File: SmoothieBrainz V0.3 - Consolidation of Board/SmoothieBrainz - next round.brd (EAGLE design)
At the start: 101 x 101 mm, 219 parts, among them IC1 LPC1769, IC5 LD117ADT33TR, Q1 BSL207SP, Q2 12MHz, SW1 SW_TACT_4P_B, SW3 SW_TACT_4P_B, T1 BC817, U3 USD-SOCKETUSD, X1 MSTBA2, X14 USBPTH, X2 GMSTBA2, X3 GMSTBA4, X4 1751248, X5 1751248, X6 1751248, X7 1751248

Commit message: more routing, almost done
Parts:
- added SJ26: (no value), SparkFun:SJ_3
- moved C13 0.32 mm to (70.2, 26.5)
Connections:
- new net V-ENDSTOP: SJ26.2, XMN.1, XMX.1, YMN.1, YMX.1, ZMN.1, ZMX.1
- net 24V: now also SJ26.3
- net 5V: now also SJ26.1; no longer XMN.1, XMX.1, YMN.1, YMX.1, ZMN.1, ZMX.1
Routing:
- net 24V: track 169.6 -> 259.8 mm, vias 1 -> 3
- net PLAY_LED: track 7.64 -> 91.6 mm, vias 0 -> 4
- net V-ENDSTOP: track 0.00 -> 47.3 mm, vias 0 -> 1
- net GND: track 390.8 -> 425.6 mm, vias 92 -> 98
- net BUZZER-RRD: track 29.9 -> 59.0 mm, vias 1 -> 3
- net P1_30_CLICK-ON-RRD: track 26.2 -> 49.5 mm, vias 1 -> 3
- net RTS: track 116.5 -> 136.0 mm
- net 3.3V: track 660.3 -> 667.0 mm
- net 5V: track 246.9 -> 240.6 mm
- net P2.9: track 28.3 -> 34.5 mm
- net 15: track 9.82 -> 12.5 mm
- net TH4: track 100.8 -> 103.2 mm
- net RESET: track 93.4 -> 92.1 mm
- net ESPRX: track 101.7 -> 100.5 mm
- net 2: track 13.8 -> 14.9 mm
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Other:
- board text added: "ENDSTOP VOLTAGE"

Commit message: Finished routing, cleanup, and DRC processing.
I just need to fix the 4 remaining motor drivers per the template
already done on the first 2.  Time for some community review.
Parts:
- moved SW1 0.33 mm to (96.2, 9.71)
- moved S1 0.08 mm to (90.0, 9.71)
- moved C34 0.08 mm to (28.3, 81.1)
- moved C31 0.08 mm to (13.1, 81.1)
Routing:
- net GND: track 425.6 -> 778.5 mm, vias 98 -> 163
- net 5V: track 240.6 -> 258.3 mm, vias 6 -> 8
- net 3.3V: track 667.0 -> 684.2 mm, vias 21 -> 23
- net EN5: track 95.3 -> 85.1 mm
- net V-ENDSTOP: track 47.3 -> 55.2 mm
- net Y_MIN: track 84.9 -> 88.6 mm
- net X_MAX: track 76.1 -> 79.8 mm
- net X_MIN: track 68.2 -> 71.2 mm
- net SD_MISO: track 112.3 -> 114.3 mm
- net 24V: track 259.8 -> 258.1 mm
- net P1_23-3RD-LARGE-FET: track 66.7 -> 68.2 mm
- net RTS: track 136.0 -> 134.5 mm
- net RESET: track 92.1 -> 91.4 mm
- net LED1: track 62.1 -> 61.5 mm

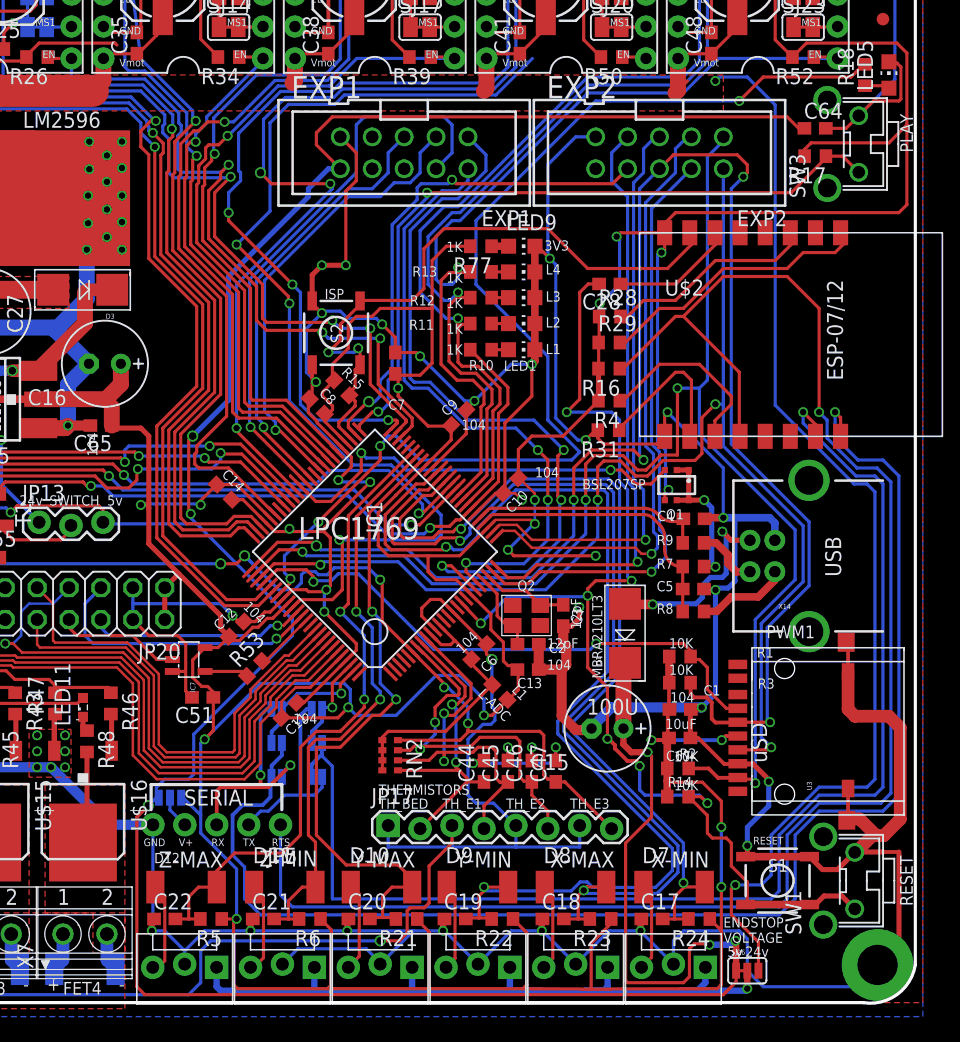
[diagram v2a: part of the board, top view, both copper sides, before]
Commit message: Servo connector added!
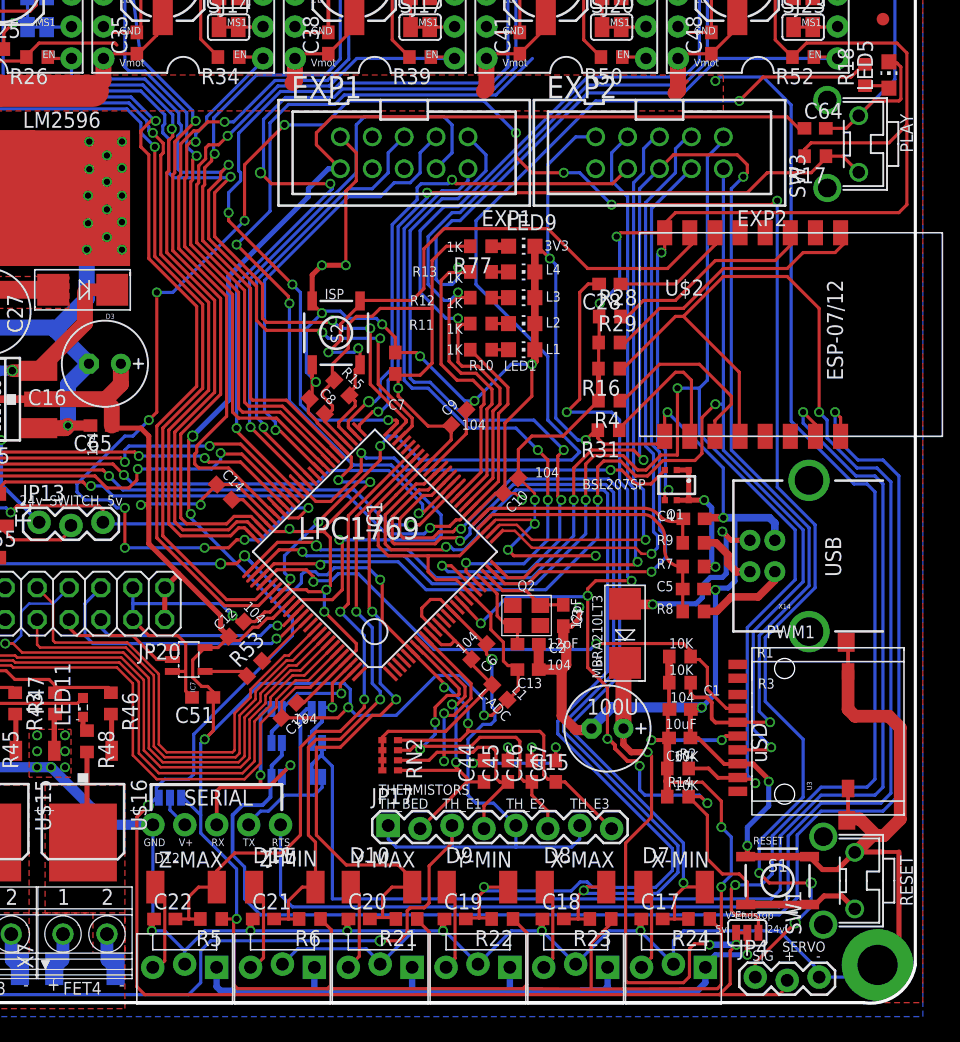
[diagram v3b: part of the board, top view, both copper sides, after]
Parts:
- added JP4: (no value), SparkFun-Connectors:1X03_LOCK
- moved SJ26 3.02 mm to (87.6, 5.56)
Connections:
- net 5V: now also JP4.2
- net GND: now also JP4.3
- net PWM0_PSU_OUT: now also JP4.1
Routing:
- net PWM0_PSU_OUT: track 0.00 -> 182.6 mm, vias 0 -> 16
- net 5V: track 258.3 -> 264.8 mm
- net GND: track 778.5 -> 776.7 mm
- net SD_SCK: track 104.5 -> 106.2 mm
- net 24V: track 258.1 -> 256.6 mm
- net SD_MOSI: track 131.5 -> 132.3 mm
- net AGND: track 159.9 -> 159.2 mm
- net 3.3V: track 684.2 -> 684.9 mm
- net SD_MISO: track 114.3 -> 114.9 mm
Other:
- board text added: "SERVO"
- board text added: "SIG"
- board text added: "V-Endstop"
- board text removed: "ENDSTOP VOLTAGE"

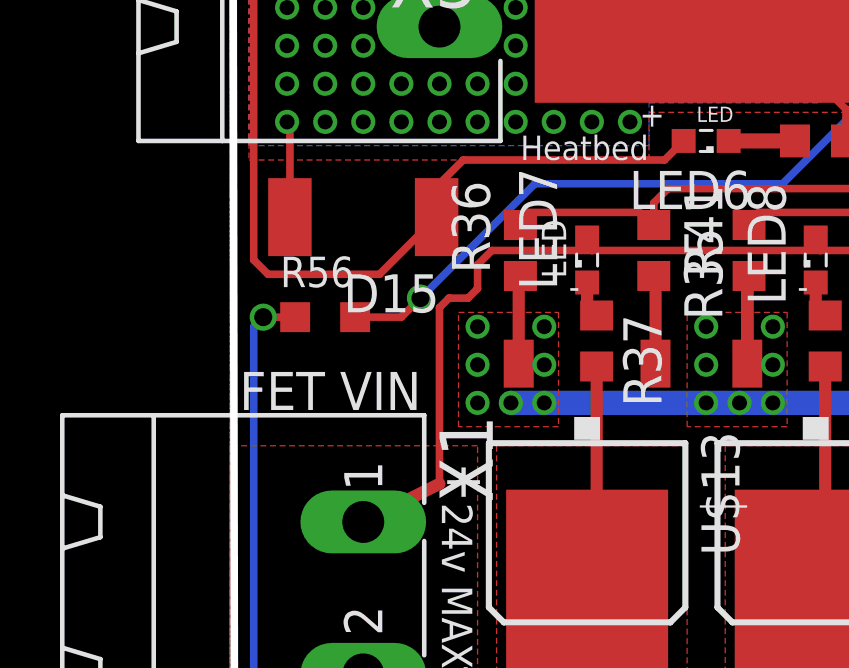
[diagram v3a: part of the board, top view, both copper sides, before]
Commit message: added solder jumper to pcb thermistor circuit
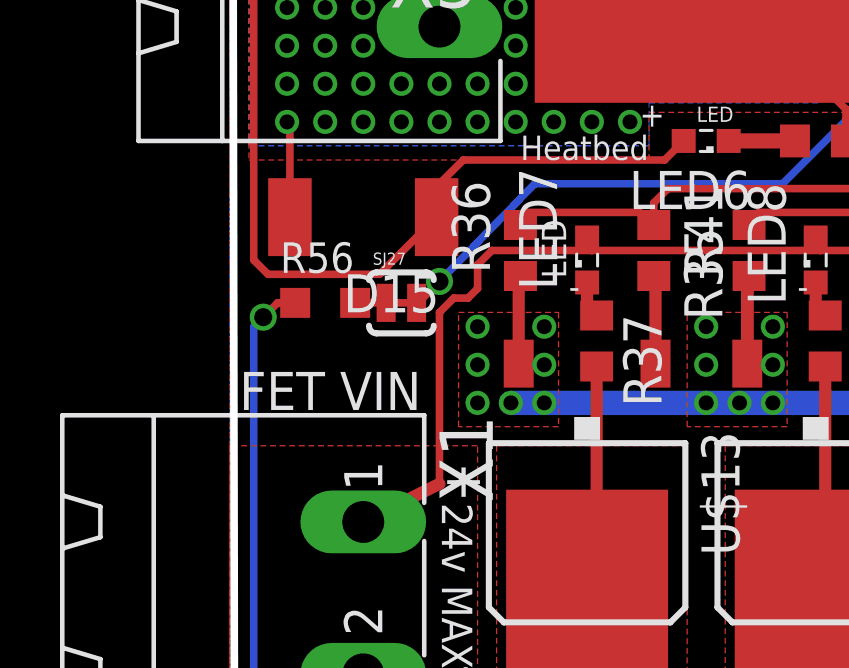
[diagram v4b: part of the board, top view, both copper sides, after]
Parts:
- added SJ27: THERM-JUMPER, SparkFun-Retired:SJ_2S-TRACE
- moved R56 0.48 mm to (3.17, 22.1)
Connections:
- net TH4: now also SJ27.1, SJ27.2
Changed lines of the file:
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@@
 <attribute name="VALUE" x="31.369" y="35.687" size="0.8128" layer="27" rot="R180"/>
 </element>
-<element name="R56" library="varistor" package="CT/CN0603" value="THERM" x="3.175" y="21.59" smashed="yes">
-<attribute name="NAME" x="1.675" y="22.59" size="1.016" layer="25"/>
-<attribute name="VALUE" x="1.04" y="22.13" size="0.8128" layer="27"/>
+<element name="R56" library="varistor" package="CT/CN0603" value="THERM" x="3.175" y="22.06625" smashed="yes">
+<attribute name="NAME" x="1.675" y="23.06625" size="1.016" layer="25"/>
+<attribute name="VALUE" x="0.484375" y="22.60625" size="0.8128" layer="27"/>
 </element>
 <element name="SJ26" library="SparkFun" package="SJ_3" value="" x="87.63" y="5.55625"/>
 <element name="JP4" library="SparkFun-Connectors" package="1X03_LOCK" value="" x="88.265" y="1.905"/>
+<element name="SJ27" library="SparkFun-Retired" package="SJ_2S-TRACE" value="THERM-JUMPER" x="5.715" y="22.06625" smashed="yes">
+<attribute name="NAME" x="4.7625" y="23.33625" size="0.4064" layer="25"/>
+<attribute name="VALUE" x="2.38125" y="20.41525" size="0.4064" layer="27"/>
+</element>
 </elements>
 <signals>
@@
 <wire x1="63.5" y1="25.0825" x2="63.8175" y2="25.0825" width="0.254" layer="16"/>
 <contactref element="R56" pad="2"/>
-<wire x1="5.715" y1="21.59" x2="4.175" y2="21.59" width="0.254" layer="1"/>
-<wire x1="6.35" y1="22.225" x2="5.715" y2="21.59" width="0.254" layer="1"/>
-<wire x1="10.16" y1="26.035" x2="6.35" y2="22.225" width="0.254" layer="16"/>
+<wire x1="10.16" y1="26.035" x2="6.985" y2="22.780625" width="0.254" layer="16"/>
 <wire x1="18.415" y1="26.035" x2="10.16" y2="26.035" width="0.254" layer="16"/>
 <wire x1="24.13" y1="31.75" x2="18.415" y2="26.035" width="0.254" layer="16"/>
@@
 <wire x1="48.41875" y1="34.76625" x2="47.625" y2="35.56" width="0.254" layer="16"/>
 <wire x1="60.96" y1="27.94" x2="61.005203125" y2="27.933796875" width="0.254" layer="1"/>
-<via x="6.35" y="22.225" extent="1-16" drill="0.6"/>
+<via x="6.985" y="22.780625" extent="1-16" drill="0.6"/>
 <via x="45.72" y="34.925" extent="1-16" drill="0.6"/>
 <via x="47.625" y="35.56" extent="1-16" drill="0.6"/>
@@
 <wire x1="65.405" y1="21.59" x2="65.405" y2="21.510625" width="0.254" layer="1"/>
 <wire x1="65.405" y1="21.510625" x2="64.779375" y2="20.885" width="0.254" layer="1"/>
+<contactref element="SJ27" pad="2"/>
+<contactref element="SJ27" pad="1"/>
+<wire x1="5.207" y1="22.06625" x2="5.207" y2="22.066125" width="0.254" layer="1"/>
+<wire x1="5.207" y1="22.066125" x2="4.175" y2="22.06625" width="0.254" layer="1"/>
+<wire x1="5.207" y1="22.06625" x2="6.223" y2="22.06625" width="0.254" layer="1"/>
+<wire x1="6.223" y1="22.06625" x2="6.270625" y2="22.06625" width="0.254" layer="1"/>
+<wire x1="6.270625" y1="22.06625" x2="6.985" y2="22.780625" width="0.254" layer="1"/>
 </signal>
 <signal name="RTS">
@@
 <wire x1="66.877040625" y1="27.737959375" x2="67.31" y2="27.305" width="0.254" layer="1"/>
 <via x="67.31" y="27.305" extent="1-16" drill="0.6"/>
-<contactref element="R56" pad="1"/>
 <wire x1="64.135" y1="12.7" x2="62.309375" y2="10.874375" width="0.254" layer="1"/>
 <wire x1="64.135" y1="14.097" x2="64.135" y2="12.7" width="0.254" layer="1"/>
@@
 <wire x1="6.35" y1="8.255" x2="1.74625" y2="8.255" width="0.254" layer="16"/>
 <wire x1="0.79375" y1="9.2075" x2="0.79375" y2="21.2725" width="0.254" layer="16"/>
-<wire x1="2.175" y1="21.59" x2="1.905" y2="21.59" width="0.254" layer="1"/>
 <via x="1.11125" y="21.59" extent="1-16" drill="0.6"/>
-<wire x1="1.11125" y1="21.59" x2="2.175" y2="21.59" width="0.254" layer="1"/>
 <wire x1="0.79375" y1="21.2725" x2="1.11125" y2="21.59" width="0.254" layer="16"/>
 <wire x1="67.31" y1="27.305" x2="67.31" y2="23.5346875" width="0.254" layer="16"/>
@@
 <wire x1="74.295" y1="14.097" x2="74.295" y2="13.0175" width="0.254" layer="16"/>
 <wire x1="74.295" y1="13.0175" x2="73.66" y2="12.3825" width="0.254" layer="16"/>
+<contactref element="R56" pad="1"/>
+<wire x1="2.175" y1="22.06625" x2="1.5875" y2="22.06625" width="0.254" layer="1"/>
+<wire x1="1.5875" y1="22.06625" x2="1.11125" y2="21.59" width="0.254" layer="1"/>
 </signal>
 <signal name="N$23">
@@
 <vertex x="8.255" y="17.30375"/>
 </polygon>
-<wire x1="6.985" y1="21.9075" x2="6.985" y2="16.03375" width="0.254" layer="1"/>
+<wire x1="6.985" y1="21.74875" x2="6.985" y2="16.03375" width="0.254" layer="1"/>
 <wire x1="6.985" y1="16.03375" x2="4.445" y2="14.76375" width="0.4064" layer="1"/>
 <contactref element="LED8" pad="A"/>
@@
 <wire x1="33.175" y1="5.45625" x2="33.175" y2="3.39375" width="1.016" layer="16"/>
 <wire x1="33.175" y1="3.39375" x2="32.48" y2="2.69875" width="1.016" layer="16"/>
-<wire x1="6.985" y1="21.9075" x2="7.3025" y2="22.225" width="0.254" layer="1"/>
-<wire x1="7.3025" y1="22.225" x2="7.9375" y2="22.225" width="0.254" layer="1"/>
+<wire x1="6.985" y1="21.74875" x2="7.46125" y2="22.225" width="0.254" layer="1"/>
+<wire x1="7.46125" y1="22.225" x2="7.9375" y2="22.225" width="0.254" layer="1"/>
 <wire x1="8.255" y1="22.5425" x2="7.9375" y2="22.225" width="0.254" layer="1"/>
 <polygon width="0.254" layer="16" isolate="0.254">

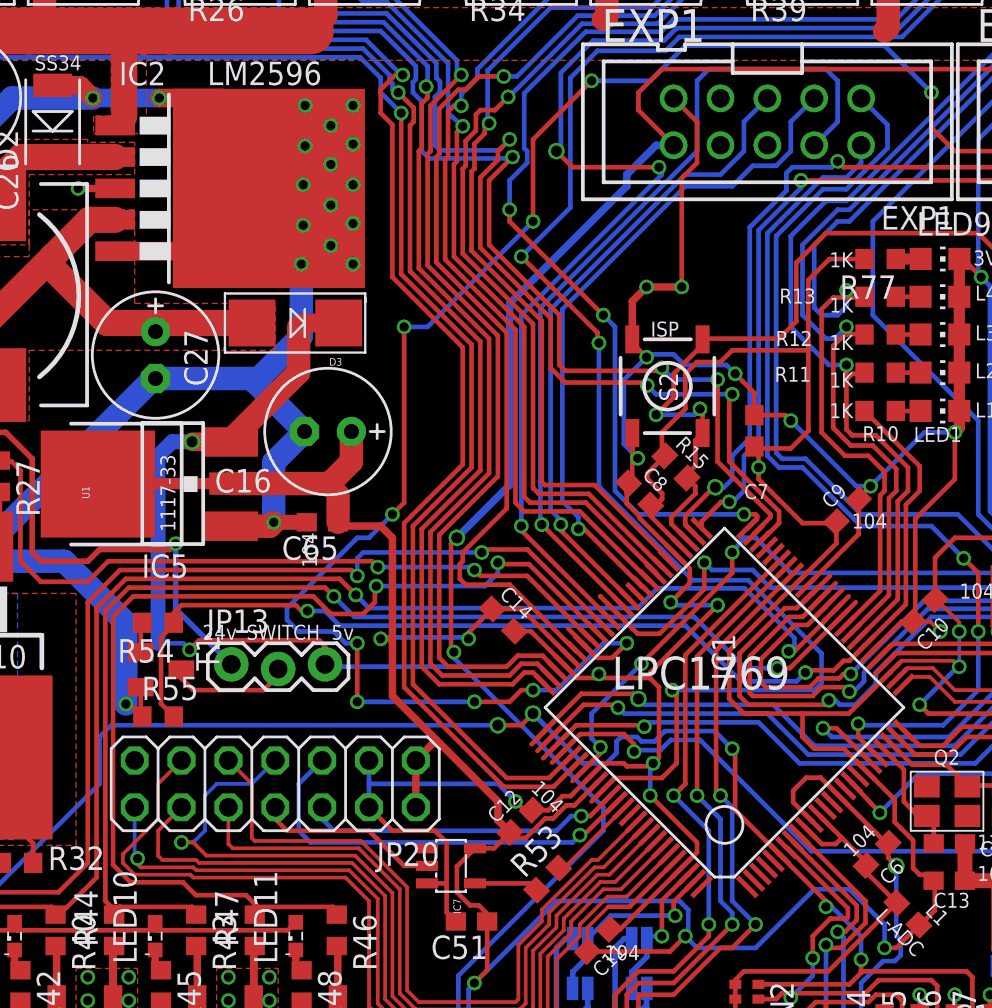
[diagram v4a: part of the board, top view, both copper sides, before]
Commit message: Routing cleaned up
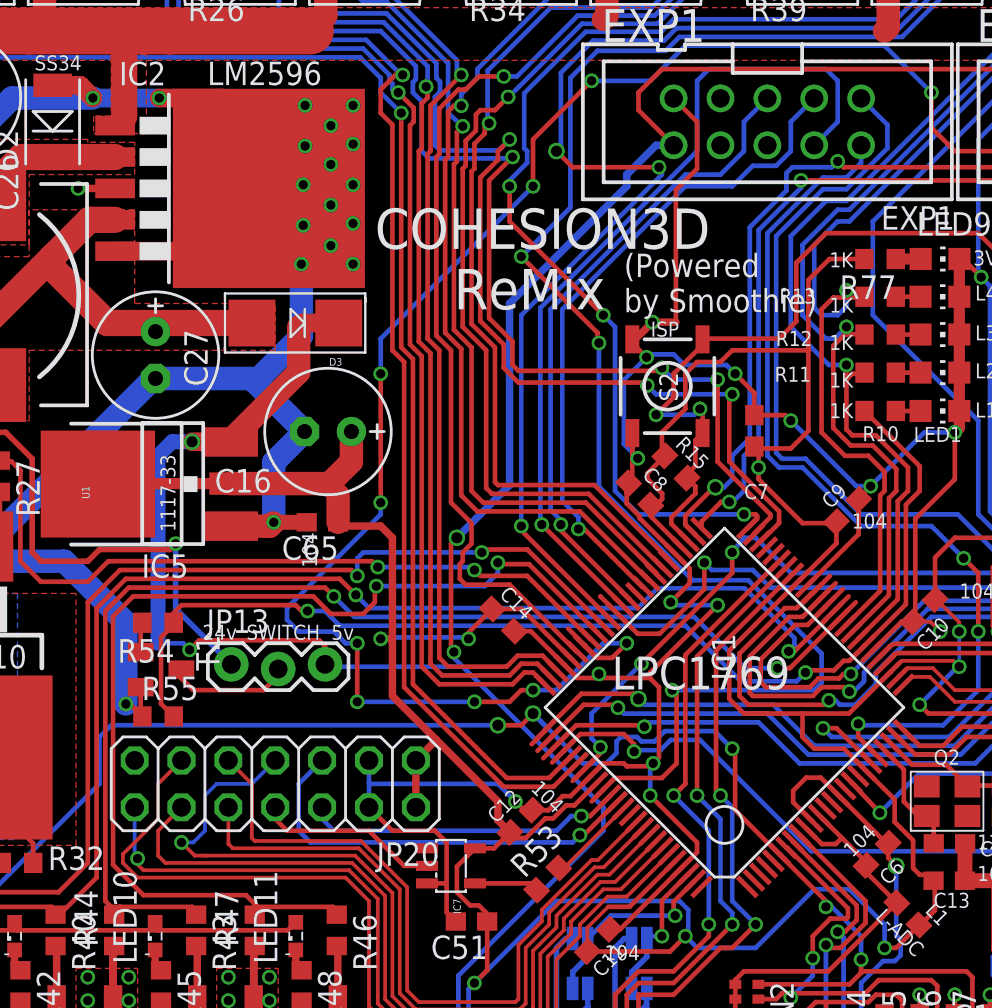
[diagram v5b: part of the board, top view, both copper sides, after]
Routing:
- net EN1: track 76.7 -> 74.1 mm
- net STP3: track 69.1 -> 66.4 mm
- net STP1: track 91.0 -> 88.3 mm
- net STP2: track 76.8 -> 74.2 mm
- net DIR1: track 98.5 -> 95.9 mm
- net STP4: track 71.1 -> 69.5 mm
- net DIR3: track 64.4 -> 65.9 mm
- net EN2: track 56.8 -> 58.3 mm
- net DIR4: track 67.0 -> 68.4 mm
- net DIR2: track 79.9 -> 81.4 mm
- net EN3: track 43.7 -> 45.2 mm
- net EN4: track 55.7 -> 57.1 mm
- net PWM0_PSU_OUT: track 182.6 -> 181.5 mm
- net GND: track 776.7 -> 776.5 mm, vias 163 -> 162
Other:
- board text added: "(Powered by Smoothie)"
- board text added: "COHESION3D ReMix"
